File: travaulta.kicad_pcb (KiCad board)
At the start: 2 copper layers, 209.7 x 76.4 mm, 121 parts, among them J1 USB_C_Receptacle_USB2.0, J2 JST, Q1 2N7002, Q2 2N7002, SW1 EC_SW, SW10 EC_SW, SW11 EC_SW, SW12 EC_SW, SW13 EC_SW, SW14 EC_SW, SW15 EC_SW, SW16 EC_SW, SW17 EC_SW, SW18 EC_SW, SW19 EC_SW, SW2 EC_SW, SW20 EC_SW, SW21 EC_SW, SW22 EC_SW, SW23 EC_SW, SW24 EC_SW, SW25 EC_SW, SW26 EC_SW, SW27 EC_SW, SW28 EC_SW, SW29 EC_SW, SW3 EC_SW, SW30 EC_SW, SW31 EC_SW, SW32 EC_SW, SW33 EC_SW, SW34 EC_SW, SW35 EC_SW, SW36 EC_SW, SW37 EC_SW, SW38 SW_MEC_5G, SW4 EC_SW, SW5 EC_SW, SW6 EC_SW, SW7 EC_SW, SW8 EC_SW, SW9 EC_SW, U1 STM32F411CCUx, U2 XC6206PxxxMR, U3 74HC4051, U4 74HC4051, U5 OPA350, U6 MAX5423, Y1 16 MHz

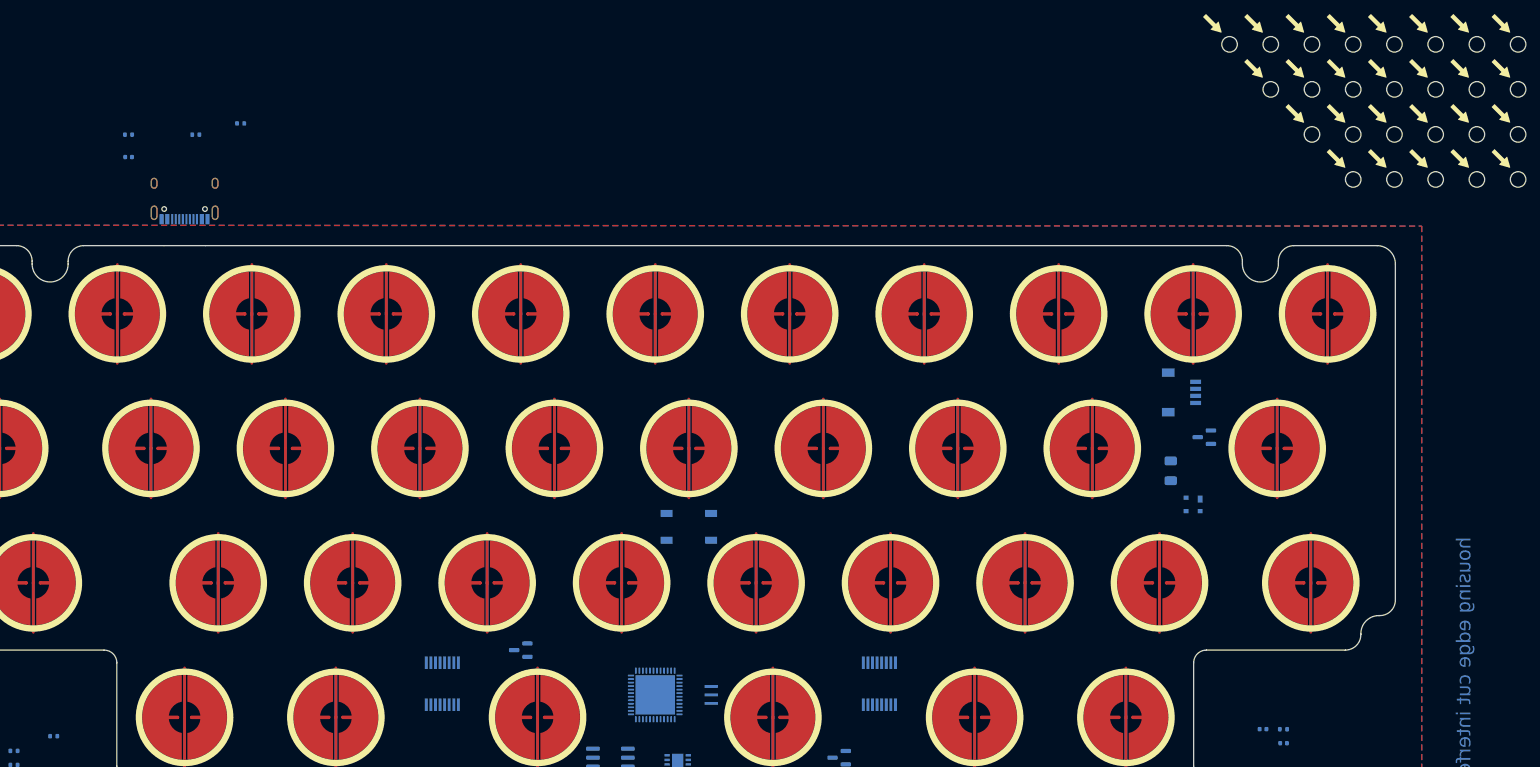
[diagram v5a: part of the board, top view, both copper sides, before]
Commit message: changed rol, col schematics /// made pcb 4 layers
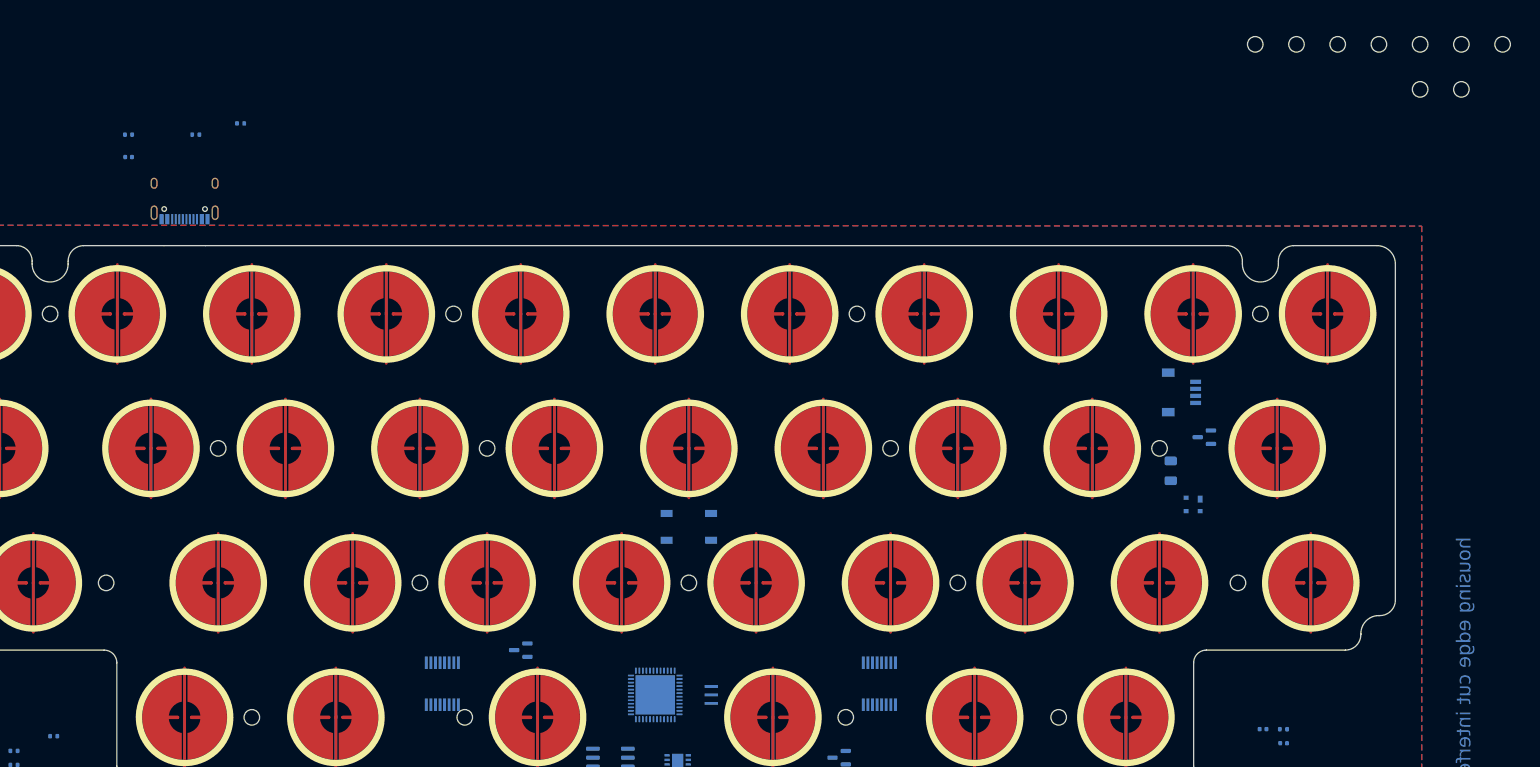
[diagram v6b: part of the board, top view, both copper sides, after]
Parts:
- H1, H10, H11, H12, H13, H14, H15, H16, H17, H18, H19, H2, H20, H21, H22, H23, H24, H25, H26, H3, H4, H5, H6, H7, H8, H9: moved to F.Cu
- moved H4 214.1 mm to (71.4, 95.2), turned to 0 degrees
- moved H6 209.5 mm to (63.5, 57.1), turned to 0 degrees
- moved H9 189.5 mm to (92.1, 114.3), turned to 0 degrees
- moved H17 185.4 mm to (87.3, 76.2), turned to 0 degrees
- moved H5 154.8 mm to (115.9, 95.2), turned to 0 degrees
- moved H14 145.7 mm to (122.2, 114.3), turned to 0 degrees
- moved H19 136.0 mm to (125.4, 76.2), turned to 0 degrees
- moved H15 128.9 mm to (120.7, 57.1), turned to 0 degrees
- moved H24 114.4 mm to (176.2, 114.3), turned to 0 degrees
- moved H1 113.6 mm to (154.0, 95.2), turned to 0 degrees
- moved H3 101.6 mm to (206.4, 114.3), turned to 0 degrees
- moved H21 92.5 mm to (182.6, 76.2), turned to 0 degrees
- moved H20 85.8 mm to (177.8, 57.1), turned to 0 degrees
- moved H8 84.2 mm to (192.1, 95.2), turned to 0 degrees
- moved H23 69.6 mm to (231.8, 95.2), turned to 0 degrees
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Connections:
- net RES_W renamed ADC
- J2 pad 1: VBUS -> VCC
- SW32 pad 2: COL2 -> COL1
- SW33 pad 2: COL3 -> COL2
- SW34 pad 2: COL4 -> COL3
- SW36 pad 2: COL6 -> COL7
- SW37 pad 2: COL7 -> COL8
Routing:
- added copper zone on In1.Cu, net GND
- added copper zone on In2.Cu, net GND
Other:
- copper layers 2 -> 4

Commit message: early routing
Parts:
- removed C_USBSHIELD1: 4.7nF, Capacitor_SMD:C_0402_1005Metric
- removed J1: USB_C_Receptacle_USB2.0, Connector_USB:USB_C_Receptacle_HRO_TYPE-C-31-M-12
- removed R_USB1, R_USB2: 5.1k, Resistor_SMD:R_0402_1005Metric
- removed R_USBSHIELD1: 1M, Resistor_SMD:R_0402_1005Metric
- added ?: , , F.Cu at (176.2, 114.3)
- added ?: , , F.Cu at (63.5, 57.1)
- added ?: , , F.Cu at (154.0, 95.2)
- added ?: , , F.Cu at (87.3, 76.2)
- added ?: , , F.Cu at (231.8, 95.2)
- added ?: , , F.Cu at (234.9, 57.1)
- added ?: , , F.Cu at (182.6, 76.2)
- added ?: , , F.Cu at (125.4, 76.2)
- added ?: , , F.Cu at (71.4, 95.2)
- added ?: , , F.Cu at (92.1, 114.3)
- added ?: , , F.Cu at (206.4, 114.3)
- added ?: , , F.Cu at (177.8, 57.1)
- added ?: , , F.Cu at (122.2, 114.3)
- added ?: , , F.Cu at (192.1, 95.2)
- added ?: , , F.Cu at (120.7, 57.1)
- added ?: , , F.Cu at (220.7, 76.2)
- moved H10 276.1 mm to (-40.8, 71.4)
- moved H23 262.7 mm to (-29.1, 65.1)
- moved H11 255.7 mm to (-35.0, 77.8)
- moved H3 239.4 mm to (-29.1, 71.4)
- moved H21 217.6 mm to (-35.0, 71.4)
- moved H8 216.1 mm to (-23.3, 77.8)
- moved H20 201.3 mm to (-23.3, 65.1)
- moved H24 199.8 mm to (-17.5, 65.1)
- moved R18 188.3 mm to (238.1, 63.0), turned to 90 degrees
- moved R16 183.2 mm to (234.9, 101.6), turned to -90 degrees
- moved H1 173.1 mm to (-17.5, 71.4)
- moved R14 159.6 mm to (214.3, 103.2), turned to -90 degrees
- moved C12 153.3 mm to (200.0, 103.2), turned to 90 degrees
- moved H19 148.8 mm to (-23.3, 71.4)
- moved H14 144.4 mm to (-17.5, 77.8)
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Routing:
- net ROW0: track 0.00 -> 330.6 mm, vias 0 -> 8
- net ROW1: track 0.00 -> 313.7 mm, vias 0 -> 8
- net ROW2: track 0.00 -> 310.5 mm, vias 0 -> 10
- net ROW3: track 0.00 -> 201.4 mm, vias 0 -> 6
- net COL3: track 0.00 -> 71.1 mm, vias 0 -> 4
- net COL7: track 0.00 -> 70.4 mm, vias 0 -> 4
- net COL1: track 0.00 -> 69.1 mm, vias 0 -> 4
- net COL8: track 0.00 -> 69.0 mm, vias 0 -> 4
- net COL2: track 0.00 -> 68.1 mm, vias 0 -> 4
- net COL5: track 0.00 -> 67.8 mm, vias 0 -> 4
- net COL0: track 0.00 -> 46.8 mm, vias 0 -> 3
- net COL9: track 0.00 -> 46.8 mm, vias 0 -> 3
- net COL4: track 0.00 -> 45.6 mm, vias 0 -> 3
- net COL6: track 0.00 -> 45.5 mm, vias 0 -> 3
- net COL10: track 0.00 -> 11.1 mm, vias 0 -> 1
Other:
- board text added: "CLEAR RED DOTS IN VIAS!!!!"
- board text added: "COL 10 alone!!!!"

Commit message: component placement
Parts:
- removed H1, H10, H11, H12, H13, H14, H15, H16, H17, H18, H19, H2, H20, H21, H22, H23, H24, H25, H26, H3, H4, H6, H7, H8, H9: MountingHole, cipulot_parts:HOLE_M2
- removed R18: 100k, Resistor_SMD:R_0402_1005Metric
- moved R6 40.1 mm to (147.6, 120.9)
- moved SW38 36.0 mm to (181.0, 111.1), turned to -90 degrees
- moved C3 32.8 mm to (180.5, 121.8), turned to 180 degrees
- moved R5 31.5 mm to (178.4, 117.6)
- moved Q1 31.2 mm to (181.0, 119.1)
- moved C2 29.1 mm to (176.5, 118.1), turned to 0 degrees
- moved C14 23.6 mm to (116.4, 118.5), turned to -90 degrees
- moved D1 14.6 mm to (226.8, 69.6)
- moved R15 12.6 mm to (98.4, 101.6)
- moved R22 11.5 mm to (112.1, 114.0), turned to 180 degrees
- moved R9 11.4 mm to (145.9, 106.7), turned to 90 degrees
- moved Q2 10.8 mm to (113.5, 116.7), turned to -90 degrees
- moved R1 10.7 mm to (144.9, 106.7), turned to 90 degrees
- moved R14 10.2 mm to (208.0, 111.1)
- moved R8 9.71 mm to (146.9, 106.7), turned to -90 degrees
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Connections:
- D1 pad 2: D- -> D+
- D1 pad 3: D+ -> D-
- R1 pad 1: Net-(R1-Pad1) -> Net-(U1-Pad25)
- R2 pad 2: Net-(R2-Pad2) -> Net-(U1-Pad28)
- R8 pad 2: SWCLK -> Net-(U1-Pad27)
- R9 pad 1: Net-(R9-Pad1) -> Net-(U1-Pad26)
- SW11 pad 2: COL10 -> COL9
- U1 pad 25: unconnected-(U1-Pad25) -> Net-(U1-Pad25)
- U1 pad 26: unconnected-(U1-Pad26) -> Net-(U1-Pad26)
- U1 pad 27: unconnected-(U1-Pad27) -> Net-(U1-Pad27)
- U1 pad 28: unconnected-(U1-Pad28) -> Net-(U1-Pad28)
- U1 pad 38: Net-(R9-Pad1) -> unconnected-(U1-Pad38)
- U1 pad 39: Net-(R1-Pad1) -> AMUX_SEL_2
- U1 pad 40: Net-(R2-Pad2) -> AMUX_SEL_1
- U1 pad 41: AMUX_SEL_2 -> AMUX_SEL_0
- U1 pad 42: AMUX_SEL_1 -> APLEX_EN_PIN_1
- U1 pad 43: AMUX_SEL_0 -> APLEX_EN_PIN_0
- U1 pad 45: APLEX_EN_PIN_1 -> unconnected-(U1-Pad45)
- U1 pad 46: APLEX_EN_PIN_0 -> unconnected-(U1-Pad46)
- U3 pad 1: COL10 -> COL9
- U3 pad 12: COL9 -> COL8
- U3 pad 13: COL6 -> COL5
- U3 pad 14: COL7 -> COL6
- U3 pad 15: COL8 -> COL7
- U4 pad 5: COL5 -> unconnected-(U4-Pad5)
- U5 pad 2: APLEX_OUT_PIN_0 -> RES_L
- U5 pad 3: RES_L -> APLEX_OUT_PIN_0
- U5 pad 4: VBAT -> GND
- U5 pad 7: GND -> VBAT
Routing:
- net ROW1: track 313.7 -> 360.5 mm, vias 8 -> 11
- net COL0: track 46.8 -> 0.00 mm, vias 3 -> 0
- net COL9: track 46.8 -> 92.4 mm, vias 3 -> 4
- net D+: track 0.00 -> 14.8 mm
- net D-: track 0.00 -> 14.2 mm
- net VBAT: track 0.00 -> 12.9 mm, vias 0 -> 3
- net COL10: track 11.1 -> 0.00 mm, vias 1 -> 0
- net ROW0: track 330.6 -> 320.1 mm
- net VCC: track 0.00 -> 9.77 mm
- net +5V: track 0.00 -> 6.20 mm
- net XTAL0: track 0.00 -> 4.75 mm
- net Net-(R4-Pad1): track 0.00 -> 3.63 mm
- net BOOT1: track 0.00 -> 3.41 mm
- net NRST: track 0.00 -> 3.25 mm
- net XTAL1: track 0.00 -> 2.62 mm
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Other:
- board text added: "something not working with the footprint, no power 3v3 at switch"
- board text removed: "COL 10 alone!!!!"
